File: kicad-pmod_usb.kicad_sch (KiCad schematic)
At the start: 14 parts, among them J2 USB_B, J3 Debug, SW1 Reset, U1 USBLC6-2SC6

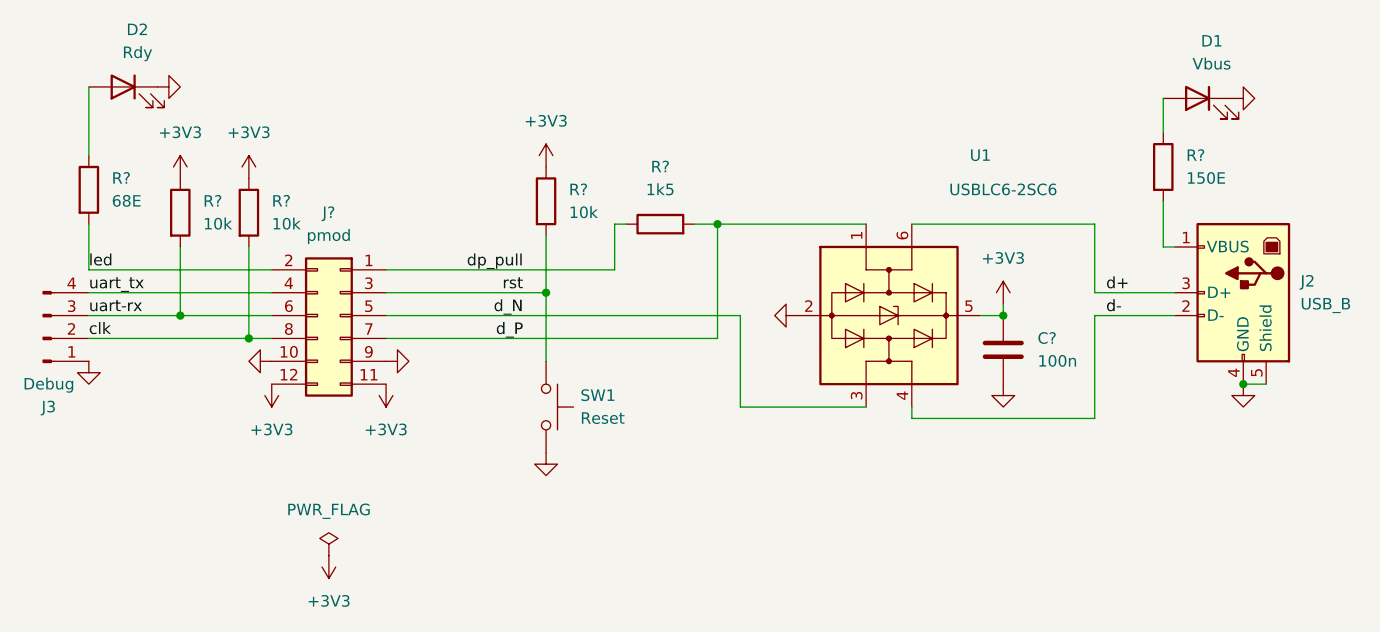
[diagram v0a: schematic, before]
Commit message: change resistor values
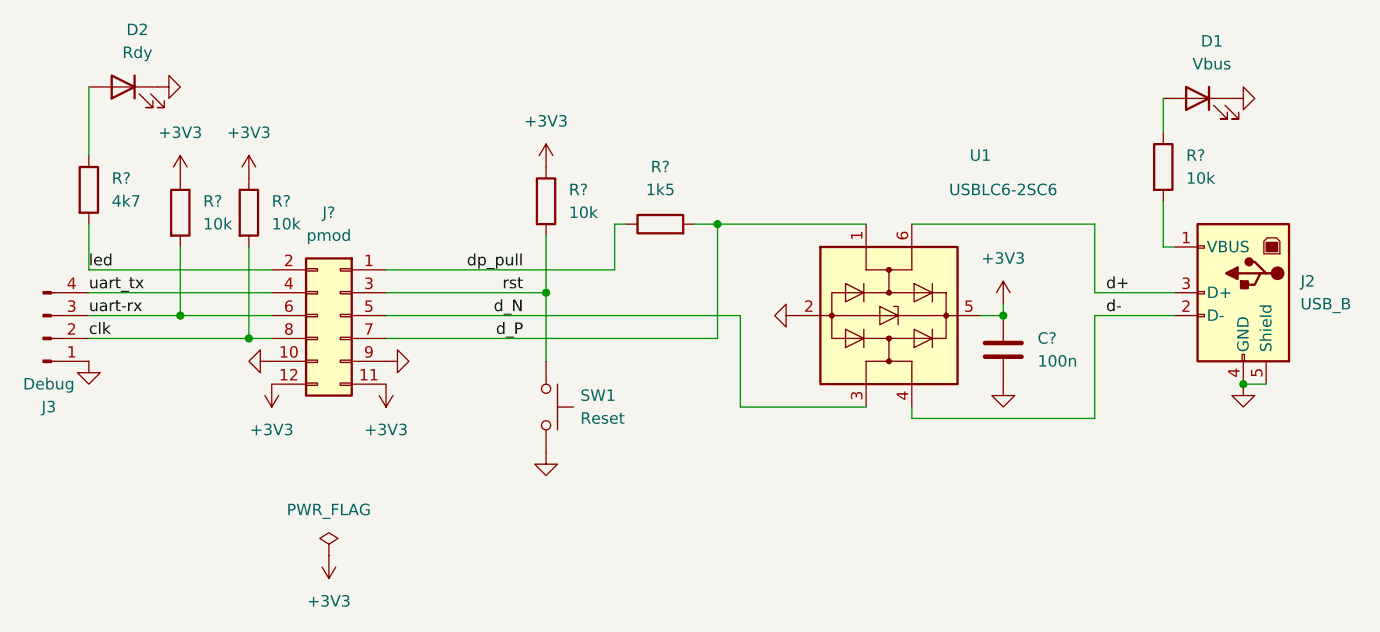
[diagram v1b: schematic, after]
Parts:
- R?: value 150E -> 10k
- R?: value 68E -> 4k7
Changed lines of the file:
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@@
       (effects (font (size 1.27 1.27)) (justify left))
     )
-    (property "Value" "150E" (at 186.69 76.2 0)
+    (property "Value" "10k" (at 186.69 76.2 0)
       (effects (font (size 1.27 1.27)) (justify left))
     )
@@
       (effects (font (size 1.27 1.27)) (justify left))
     )
-    (property "Value" "68E" (at 67.31 78.74 0)
+    (property "Value" "4k7" (at 67.31 78.74 0)
       (effects (font (size 1.27 1.27)) (justify left))
     )
